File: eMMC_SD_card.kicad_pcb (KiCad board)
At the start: 4 copper layers, 100 x 74 mm, 65 parts, among them J1 SD_Card, J2 Conn_Coaxial, U1 ESP32-PICO-D4, U2 TagConnect_TC2030_ESP32

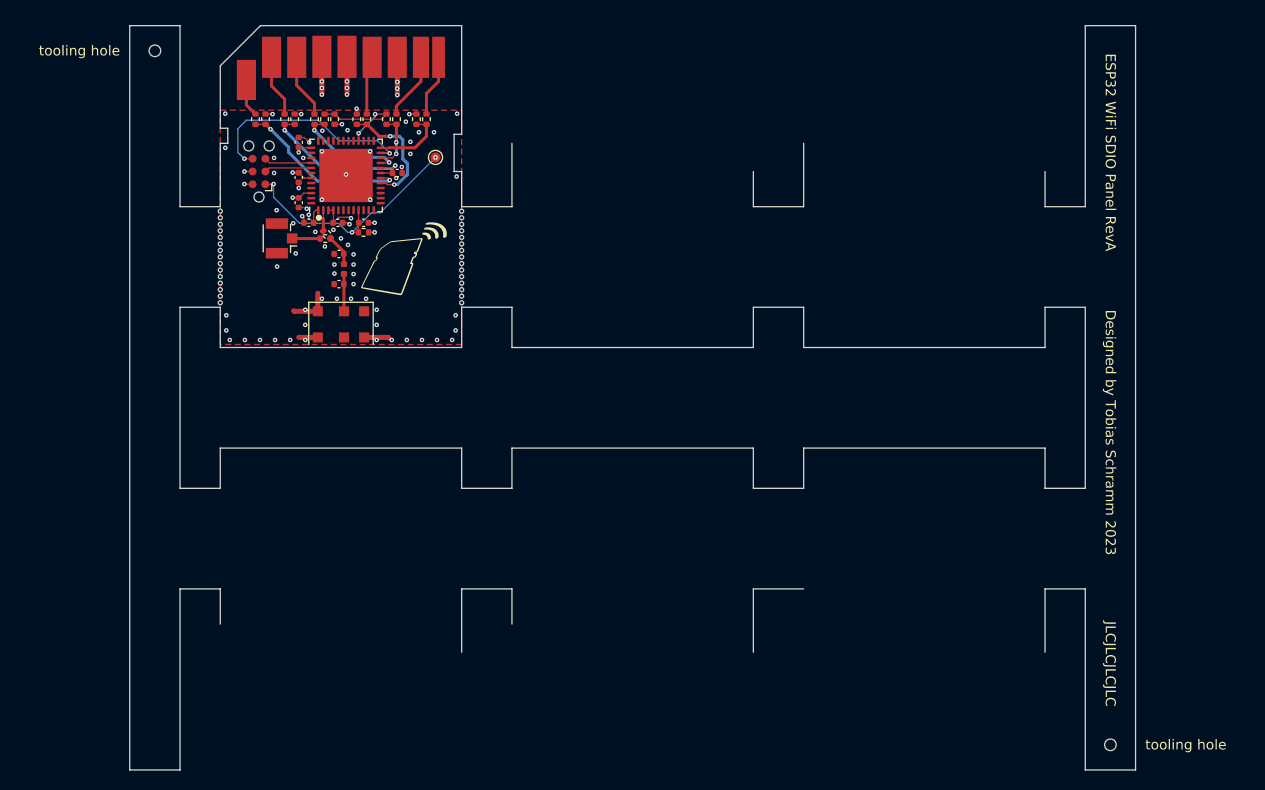
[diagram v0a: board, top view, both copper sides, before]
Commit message: Panelize
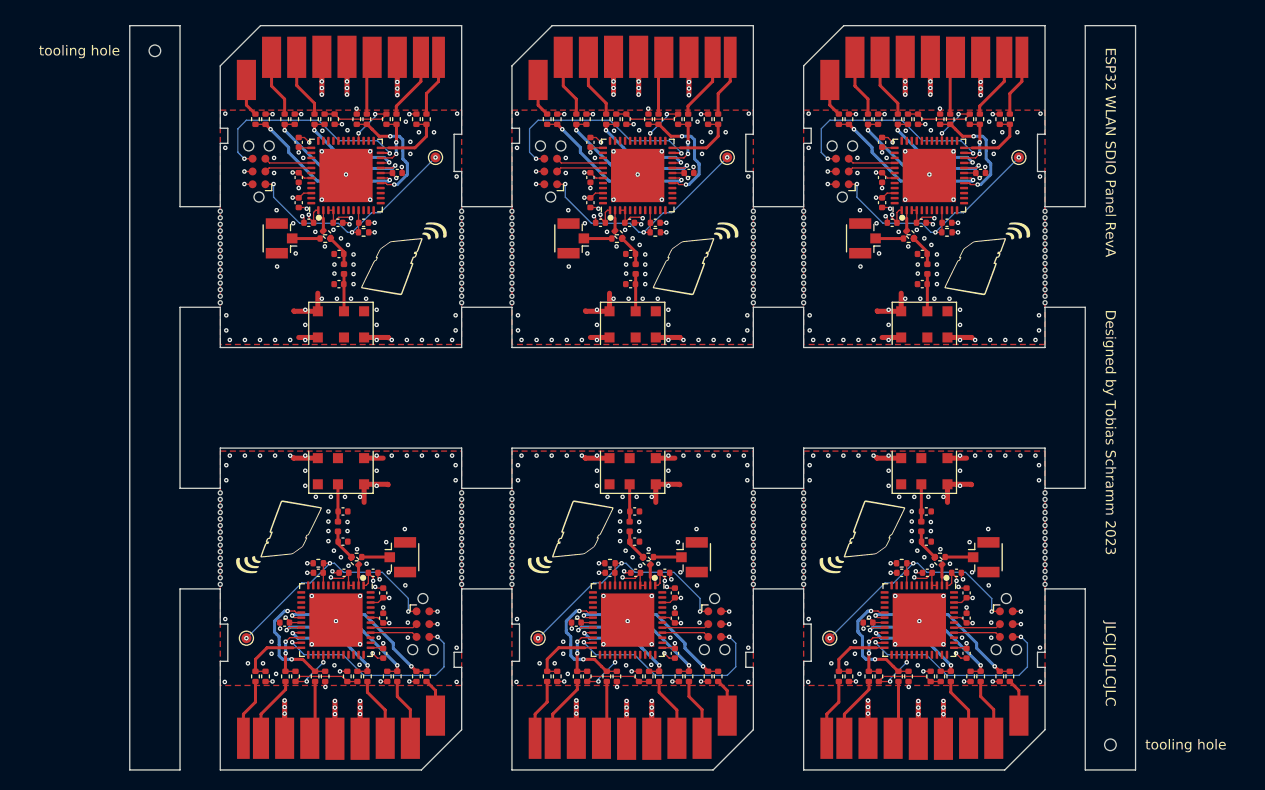
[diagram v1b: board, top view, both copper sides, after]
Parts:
- added AE2: Antenna_Chip, Antenna_antenova:SR4W035, F.Cu at (117.0, 144.3)
- added AE3: Antenna_Chip, Antenna_antenova:SR4W035, F.Cu at (175.0, 144.3)
- added AE4: Antenna_Chip, Antenna_antenova:SR4W035, F.Cu at (146.0, 129.7)
- added AE5: Antenna_Chip, Antenna_antenova:SR4W035, F.Cu at (146.0, 144.3)
- added AE6: Antenna_Chip, Antenna_antenova:SR4W035, F.Cu at (175.0, 129.7)
- added C10: 100nF, Capacitor_SMD:C_0402_1005Metric, F.Cu at (114.8, 154.4)
- added C11: 2.2uF, Capacitor_SMD:C_0402_1005Metric, F.Cu at (111.4, 159.3)
- added C12: 2.2uF, Capacitor_SMD:C_0402_1005Metric, F.Cu at (117.3, 154.4)
- added C13: 2.2uF, Capacitor_SMD:C_0402_1005Metric, F.Cu at (120.2, 154.4)
- added C14: 2.2uF, Capacitor_SMD:C_0402_1005Metric, F.Cu at (121.2, 156.4)
- added C15: 2.2uF, Capacitor_SMD:C_0402_1005Metric, F.Cu at (121.2, 158.9)
- added C16: 100nF, Capacitor_SMD:C_0402_1005Metric, F.Cu at (121.2, 162.4)
- added C17: DNP, Capacitor_SMD:C_0402_1005Metric, F.Cu at (117.2, 151.3)
- added C18: DNP, Capacitor_SMD:C_0402_1005Metric, F.Cu at (117.2, 148.3)
- added C19: 100nF, Capacitor_SMD:C_0402_1005Metric, F.Cu at (172.8, 154.4)
- added C20: 2.2uF, Capacitor_SMD:C_0402_1005Metric, F.Cu at (169.4, 159.3)
- added C21: 2.2uF, Capacitor_SMD:C_0402_1005Metric, F.Cu at (175.3, 154.4)
- added C22: 2.2uF, Capacitor_SMD:C_0402_1005Metric, F.Cu at (178.2, 154.4)
- added C23: 2.2uF, Capacitor_SMD:C_0402_1005Metric, F.Cu at (179.2, 156.4)
- added C24: 2.2uF, Capacitor_SMD:C_0402_1005Metric, F.Cu at (179.2, 158.9)
- added C25: 100nF, Capacitor_SMD:C_0402_1005Metric, F.Cu at (179.2, 162.4)
- added C26: DNP, Capacitor_SMD:C_0402_1005Metric, F.Cu at (175.2, 151.3)
- added C27: DNP, Capacitor_SMD:C_0402_1005Metric, F.Cu at (175.2, 148.3)
- added C28: 100nF, Capacitor_SMD:C_0402_1005Metric, F.Cu at (148.2, 119.6)
- added C29: 2.2uF, Capacitor_SMD:C_0402_1005Metric, F.Cu at (151.6, 114.7)
- added C30: 2.2uF, Capacitor_SMD:C_0402_1005Metric, F.Cu at (145.7, 119.6)
- added C31: 2.2uF, Capacitor_SMD:C_0402_1005Metric, F.Cu at (142.8, 119.6)
- added C32: 2.2uF, Capacitor_SMD:C_0402_1005Metric, F.Cu at (141.8, 117.6)
- added C33: 2.2uF, Capacitor_SMD:C_0402_1005Metric, F.Cu at (141.8, 115.1)
- added C34: 100nF, Capacitor_SMD:C_0402_1005Metric, F.Cu at (141.8, 111.6)
- added C35: DNP, Capacitor_SMD:C_0402_1005Metric, F.Cu at (145.8, 122.7)
- added C36: DNP, Capacitor_SMD:C_0402_1005Metric, F.Cu at (145.8, 125.7)
- added C37: 100nF, Capacitor_SMD:C_0402_1005Metric, F.Cu at (143.8, 154.4)
- added C38: 2.2uF, Capacitor_SMD:C_0402_1005Metric, F.Cu at (140.4, 159.3)
- added C39: 2.2uF, Capacitor_SMD:C_0402_1005Metric, F.Cu at (146.3, 154.4)
- added C40: 2.2uF, Capacitor_SMD:C_0402_1005Metric, F.Cu at (149.2, 154.4)
- added C41: 2.2uF, Capacitor_SMD:C_0402_1005Metric, F.Cu at (150.2, 156.4)
- added C42: 2.2uF, Capacitor_SMD:C_0402_1005Metric, F.Cu at (150.2, 158.9)
- added C43: 100nF, Capacitor_SMD:C_0402_1005Metric, F.Cu at (150.2, 162.4)
- added C44: DNP, Capacitor_SMD:C_0402_1005Metric, F.Cu at (146.2, 151.3)
- added C45: DNP, Capacitor_SMD:C_0402_1005Metric, F.Cu at (146.2, 148.3)
- added C46: 100nF, Capacitor_SMD:C_0402_1005Metric, F.Cu at (177.2, 119.6)
- added C47: 2.2uF, Capacitor_SMD:C_0402_1005Metric, F.Cu at (180.6, 114.7)
- added C48: 2.2uF, Capacitor_SMD:C_0402_1005Metric, F.Cu at (174.7, 119.6)
- added C49: 2.2uF, Capacitor_SMD:C_0402_1005Metric, F.Cu at (171.8, 119.6)
- added C50: 2.2uF, Capacitor_SMD:C_0402_1005Metric, F.Cu at (170.8, 117.6)
- added C51: 2.2uF, Capacitor_SMD:C_0402_1005Metric, F.Cu at (170.8, 115.1)
- added C52: 100nF, Capacitor_SMD:C_0402_1005Metric, F.Cu at (170.8, 111.6)
- added C53: DNP, Capacitor_SMD:C_0402_1005Metric, F.Cu at (174.8, 122.7)
- added C54: DNP, Capacitor_SMD:C_0402_1005Metric, F.Cu at (174.8, 125.7)
- added G***: LOGO, Icons:wlan_sd, F.Cu at (168.8, 150.8)
- added G***1: LOGO, Icons:wlan_sd, F.Cu at (139.8, 150.8)
- added G***1: LOGO, Icons:wlan_sd, F.Cu at (152.2, 123.2)
- added G***2: LOGO, Icons:wlan_sd, F.Cu at (110.8, 150.8)
- added G***2: LOGO, Icons:wlan_sd, F.Cu at (181.2, 123.2)
- added H100: MountingHole, Perforation:Perforation_0.4mm, F.Cu at (158.0, 121.0)
- added H101: MountingHole, Perforation:Perforation_0.4mm, F.Cu at (134.0, 121.7)
- added H102: MountingHole, Perforation:Perforation_0.4mm, F.Cu at (134.0, 122.3)
- added H103: MountingHole, Perforation:Perforation_0.4mm, F.Cu at (134.0, 123.0)
- added H104: MountingHole, Perforation:Perforation_0.4mm, F.Cu at (134.0, 123.7)
- added H105: MountingHole, Perforation:Perforation_0.4mm, F.Cu at (134.0, 124.3)
- added H106: MountingHole, Perforation:Perforation_0.4mm, F.Cu at (158.0, 121.7)
- added H107: MountingHole, Perforation:Perforation_0.4mm, F.Cu at (158.0, 122.3)
- added H108: MountingHole, Perforation:Perforation_0.4mm, F.Cu at (158.0, 123.0)
- added H109: MountingHole, Perforation:Perforation_0.4mm, F.Cu at (158.0, 123.7)
- added H110: MountingHole, Perforation:Perforation_0.4mm, F.Cu at (158.0, 124.3)
- added H111: MountingHole, Perforation:Perforation_0.4mm, F.Cu at (134.0, 125.0)
- added H112: MountingHole, Perforation:Perforation_0.4mm, F.Cu at (134.0, 125.6)
- added H113: MountingHole, Perforation:Perforation_0.4mm, F.Cu at (134.0, 126.2)
- added H114: MountingHole, Perforation:Perforation_0.4mm, F.Cu at (134.0, 126.9)
- added H115: MountingHole, Perforation:Perforation_0.4mm, F.Cu at (134.0, 127.5)
- added H116: MountingHole, Perforation:Perforation_0.4mm, F.Cu at (158.0, 125.0)
- added H117: MountingHole, Perforation:Perforation_0.4mm, F.Cu at (158.0, 125.6)
- added H118: MountingHole, Perforation:Perforation_0.4mm, F.Cu at (158.0, 126.2)
- added H119: MountingHole, Perforation:Perforation_0.4mm, F.Cu at (158.0, 126.9)
- added H120: MountingHole, Perforation:Perforation_0.4mm, F.Cu at (158.0, 127.5)
- added H121: MountingHole, Perforation:Perforation_0.4mm, F.Cu at (158.0, 155.6)
- added H122: MountingHole, Perforation:Perforation_0.4mm, F.Cu at (158.0, 154.9)
- added H123: MountingHole, Perforation:Perforation_0.4mm, F.Cu at (158.0, 154.2)
- added H124: MountingHole, Perforation:Perforation_0.4mm, F.Cu at (158.0, 153.6)
- added H125: MountingHole, Perforation:Perforation_0.4mm, F.Cu at (158.0, 152.9)
- added H126: MountingHole, Perforation:Perforation_0.4mm, F.Cu at (134.0, 155.6)
- added H127: MountingHole, Perforation:Perforation_0.4mm, F.Cu at (134.0, 154.9)
- added H128: MountingHole, Perforation:Perforation_0.4mm, F.Cu at (134.0, 154.2)
- added H129: MountingHole, Perforation:Perforation_0.4mm, F.Cu at (134.0, 153.6)
- added H130: MountingHole, Perforation:Perforation_0.4mm, F.Cu at (134.0, 152.9)
- added H131: MountingHole, Perforation:Perforation_0.4mm, F.Cu at (158.0, 152.3)
- added H132: MountingHole, Perforation:Perforation_0.4mm, F.Cu at (158.0, 151.7)
- added H133: MountingHole, Perforation:Perforation_0.4mm, F.Cu at (158.0, 151.0)
- added H134: MountingHole, Perforation:Perforation_0.4mm, F.Cu at (158.0, 150.3)
- added H135: MountingHole, Perforation:Perforation_0.4mm, F.Cu at (158.0, 149.7)
- added H136: MountingHole, Perforation:Perforation_0.4mm, F.Cu at (134.0, 152.3)
- added H137: MountingHole, Perforation:Perforation_0.4mm, F.Cu at (134.0, 151.7)
- added H138: MountingHole, Perforation:Perforation_0.4mm, F.Cu at (134.0, 151.0)
- added H139: MountingHole, Perforation:Perforation_0.4mm, F.Cu at (134.0, 150.3)
- added H140: MountingHole, Perforation:Perforation_0.4mm, F.Cu at (134.0, 149.7)
- added H141: MountingHole, Perforation:Perforation_0.4mm, F.Cu at (158.0, 149.1)
- added H142: MountingHole, Perforation:Perforation_0.4mm, F.Cu at (158.0, 148.4)
- added H143: MountingHole, Perforation:Perforation_0.4mm, F.Cu at (158.0, 147.8)
- added H144: MountingHole, Perforation:Perforation_0.4mm, F.Cu at (158.0, 147.1)
- added H145: MountingHole, Perforation:Perforation_0.4mm, F.Cu at (158.0, 146.4)
- added H146: MountingHole, Perforation:Perforation_0.4mm, F.Cu at (134.0, 149.1)
- added H147: MountingHole, Perforation:Perforation_0.4mm, F.Cu at (134.0, 148.4)
- added H148: MountingHole, Perforation:Perforation_0.4mm, F.Cu at (134.0, 147.8)
- added H149: MountingHole, Perforation:Perforation_0.4mm, F.Cu at (134.0, 147.1)
- added H150: MountingHole, Perforation:Perforation_0.4mm, F.Cu at (134.0, 146.4)
- added H151: MountingHole, Perforation:Perforation_0.4mm, F.Cu at (163.0, 118.5)
- added H152: MountingHole, Perforation:Perforation_0.4mm, F.Cu at (163.0, 119.1)
- added H153: MountingHole, Perforation:Perforation_0.4mm, F.Cu at (163.0, 119.8)
- added H154: MountingHole, Perforation:Perforation_0.4mm, F.Cu at (163.0, 120.4)
- added H155: MountingHole, Perforation:Perforation_0.4mm, F.Cu at (163.0, 121.0)
- added H156: MountingHole, Perforation:Perforation_0.4mm, F.Cu at (187.0, 118.5)
- added H157: MountingHole, Perforation:Perforation_0.4mm, F.Cu at (187.0, 119.1)
- added H158: MountingHole, Perforation:Perforation_0.4mm, F.Cu at (187.0, 119.8)
- added H159: MountingHole, Perforation:Perforation_0.4mm, F.Cu at (187.0, 120.4)
- added H160: MountingHole, Perforation:Perforation_0.4mm, F.Cu at (187.0, 121.0)
- added H161: MountingHole, Perforation:Perforation_0.4mm, F.Cu at (163.0, 121.7)
- added H162: MountingHole, Perforation:Perforation_0.4mm, F.Cu at (163.0, 122.3)
- added H163: MountingHole, Perforation:Perforation_0.4mm, F.Cu at (163.0, 123.0)
- added H164: MountingHole, Perforation:Perforation_0.4mm, F.Cu at (163.0, 123.7)
- added H165: MountingHole, Perforation:Perforation_0.4mm, F.Cu at (163.0, 124.3)
- added H166: MountingHole, Perforation:Perforation_0.4mm, F.Cu at (187.0, 121.7)
- added H167: MountingHole, Perforation:Perforation_0.4mm, F.Cu at (187.0, 122.3)
- added H168: MountingHole, Perforation:Perforation_0.4mm, F.Cu at (187.0, 123.0)
- added H169: MountingHole, Perforation:Perforation_0.4mm, F.Cu at (187.0, 123.7)
- added H170: MountingHole, Perforation:Perforation_0.4mm, F.Cu at (187.0, 124.3)
- added H171: MountingHole, Perforation:Perforation_0.4mm, F.Cu at (163.0, 125.0)
- added H172: MountingHole, Perforation:Perforation_0.4mm, F.Cu at (163.0, 125.6)
- added H173: MountingHole, Perforation:Perforation_0.4mm, F.Cu at (163.0, 126.2)
- added H174: MountingHole, Perforation:Perforation_0.4mm, F.Cu at (163.0, 126.9)
- added H175: MountingHole, Perforation:Perforation_0.4mm, F.Cu at (163.0, 127.5)
- added H176: MountingHole, Perforation:Perforation_0.4mm, F.Cu at (187.0, 125.0)
- added H177: MountingHole, Perforation:Perforation_0.4mm, F.Cu at (187.0, 125.6)
- added H178: MountingHole, Perforation:Perforation_0.4mm, F.Cu at (187.0, 126.2)
- added H179: MountingHole, Perforation:Perforation_0.4mm, F.Cu at (187.0, 126.9)
- added H180: MountingHole, Perforation:Perforation_0.4mm, F.Cu at (187.0, 127.5)
- added H31: MountingHole, Perforation:Perforation_0.4mm, F.Cu at (129.0, 155.6)
- added H32: MountingHole, Perforation:Perforation_0.4mm, F.Cu at (129.0, 154.9)
- added H33: MountingHole, Perforation:Perforation_0.4mm, F.Cu at (129.0, 154.2)
- added H34: MountingHole, Perforation:Perforation_0.4mm, F.Cu at (129.0, 153.6)
- added H35: MountingHole, Perforation:Perforation_0.4mm, F.Cu at (129.0, 152.9)
- added H36: MountingHole, Perforation:Perforation_0.4mm, F.Cu at (105.0, 155.6)
- added H37: MountingHole, Perforation:Perforation_0.4mm, F.Cu at (105.0, 154.9)
- added H38: MountingHole, Perforation:Perforation_0.4mm, F.Cu at (105.0, 154.2)
- added H39: MountingHole, Perforation:Perforation_0.4mm, F.Cu at (105.0, 153.6)
- added H40: MountingHole, Perforation:Perforation_0.4mm, F.Cu at (105.0, 152.9)
- added H41: MountingHole, Perforation:Perforation_0.4mm, F.Cu at (129.0, 152.3)
- added H42: MountingHole, Perforation:Perforation_0.4mm, F.Cu at (129.0, 151.7)
- added H43: MountingHole, Perforation:Perforation_0.4mm, F.Cu at (129.0, 151.0)
- added H44: MountingHole, Perforation:Perforation_0.4mm, F.Cu at (129.0, 150.3)
- added H45: MountingHole, Perforation:Perforation_0.4mm, F.Cu at (129.0, 149.7)
- added H46: MountingHole, Perforation:Perforation_0.4mm, F.Cu at (105.0, 152.3)
- added H47: MountingHole, Perforation:Perforation_0.4mm, F.Cu at (105.0, 151.7)
- added H48: MountingHole, Perforation:Perforation_0.4mm, F.Cu at (105.0, 151.0)
- added H49: MountingHole, Perforation:Perforation_0.4mm, F.Cu at (105.0, 150.3)
- added H50: MountingHole, Perforation:Perforation_0.4mm, F.Cu at (105.0, 149.7)
- added H51: MountingHole, Perforation:Perforation_0.4mm, F.Cu at (129.0, 149.1)
- added H52: MountingHole, Perforation:Perforation_0.4mm, F.Cu at (129.0, 148.4)
- added H53: MountingHole, Perforation:Perforation_0.4mm, F.Cu at (129.0, 147.8)
- added H54: MountingHole, Perforation:Perforation_0.4mm, F.Cu at (129.0, 147.1)
- added H55: MountingHole, Perforation:Perforation_0.4mm, F.Cu at (129.0, 146.4)
- added H56: MountingHole, Perforation:Perforation_0.4mm, F.Cu at (105.0, 149.1)
- added H57: MountingHole, Perforation:Perforation_0.4mm, F.Cu at (105.0, 148.4)
- added H58: MountingHole, Perforation:Perforation_0.4mm, F.Cu at (105.0, 147.8)
- added H59: MountingHole, Perforation:Perforation_0.4mm, F.Cu at (105.0, 147.1)
- added H60: MountingHole, Perforation:Perforation_0.4mm, F.Cu at (105.0, 146.4)
- added H61: MountingHole, Perforation:Perforation_0.4mm, F.Cu at (187.0, 155.6)
- added H62: MountingHole, Perforation:Perforation_0.4mm, F.Cu at (187.0, 154.9)
- added H63: MountingHole, Perforation:Perforation_0.4mm, F.Cu at (187.0, 154.2)
- added H64: MountingHole, Perforation:Perforation_0.4mm, F.Cu at (187.0, 153.6)
- added H65: MountingHole, Perforation:Perforation_0.4mm, F.Cu at (187.0, 152.9)
- added H66: MountingHole, Perforation:Perforation_0.4mm, F.Cu at (163.0, 155.6)
- added H67: MountingHole, Perforation:Perforation_0.4mm, F.Cu at (163.0, 154.9)
- added H68: MountingHole, Perforation:Perforation_0.4mm, F.Cu at (163.0, 154.2)
- added H69: MountingHole, Perforation:Perforation_0.4mm, F.Cu at (163.0, 153.6)
- added H70: MountingHole, Perforation:Perforation_0.4mm, F.Cu at (163.0, 152.9)
- added H71: MountingHole, Perforation:Perforation_0.4mm, F.Cu at (187.0, 152.3)
- added H72: MountingHole, Perforation:Perforation_0.4mm, F.Cu at (187.0, 151.7)
- added H73: MountingHole, Perforation:Perforation_0.4mm, F.Cu at (187.0, 151.0)
- added H74: MountingHole, Perforation:Perforation_0.4mm, F.Cu at (187.0, 150.3)
- added H75: MountingHole, Perforation:Perforation_0.4mm, F.Cu at (187.0, 149.7)
- added H76: MountingHole, Perforation:Perforation_0.4mm, F.Cu at (163.0, 152.3)
- added H77: MountingHole, Perforation:Perforation_0.4mm, F.Cu at (163.0, 151.7)
- added H78: MountingHole, Perforation:Perforation_0.4mm, F.Cu at (163.0, 151.0)
- added H79: MountingHole, Perforation:Perforation_0.4mm, F.Cu at (163.0, 150.3)
- added H80: MountingHole, Perforation:Perforation_0.4mm, F.Cu at (163.0, 149.7)
- added H81: MountingHole, Perforation:Perforation_0.4mm, F.Cu at (187.0, 149.1)
- added H82: MountingHole, Perforation:Perforation_0.4mm, F.Cu at (187.0, 148.4)
- added H83: MountingHole, Perforation:Perforation_0.4mm, F.Cu at (187.0, 147.8)
- added H84: MountingHole, Perforation:Perforation_0.4mm, F.Cu at (187.0, 147.1)
- added H85: MountingHole, Perforation:Perforation_0.4mm, F.Cu at (187.0, 146.4)
- added H86: MountingHole, Perforation:Perforation_0.4mm, F.Cu at (163.0, 149.1)
- added H87: MountingHole, Perforation:Perforation_0.4mm, F.Cu at (163.0, 148.4)
- added H88: MountingHole, Perforation:Perforation_0.4mm, F.Cu at (163.0, 147.8)
- added H89: MountingHole, Perforation:Perforation_0.4mm, F.Cu at (163.0, 147.1)
- added H90: MountingHole, Perforation:Perforation_0.4mm, F.Cu at (163.0, 146.4)
- added H91: MountingHole, Perforation:Perforation_0.4mm, F.Cu at (134.0, 118.5)
- added H92: MountingHole, Perforation:Perforation_0.4mm, F.Cu at (134.0, 119.1)
- added H93: MountingHole, Perforation:Perforation_0.4mm, F.Cu at (134.0, 119.8)
- added H94: MountingHole, Perforation:Perforation_0.4mm, F.Cu at (134.0, 120.4)
- added H95: MountingHole, Perforation:Perforation_0.4mm, F.Cu at (134.0, 121.0)
- added H96: MountingHole, Perforation:Perforation_0.4mm, F.Cu at (158.0, 118.5)
- added H97: MountingHole, Perforation:Perforation_0.4mm, F.Cu at (158.0, 119.1)
- added H98: MountingHole, Perforation:Perforation_0.4mm, F.Cu at (158.0, 119.8)
- added H99: MountingHole, Perforation:Perforation_0.4mm, F.Cu at (158.0, 120.4)
- added J10: Conn_Coaxial, Connector_Coaxial:U.FL_Hirose_U.FL-R-SMT-1_Vertical, F.Cu at (151.9, 152.8)
- added J11: SD_Card, Connector_PCB_Edge_SD:SD, F.Cu at (163.0, 100.0)
- added J12: Conn_Coaxial, Connector_Coaxial:U.FL_Hirose_U.FL-R-SMT-1_Vertical, F.Cu at (169.1, 121.2)
- added J3: SD_Card, Connector_PCB_Edge_SD:SD, F.Cu at (129.0, 174.0)
- added J4: Conn_Coaxial, Connector_Coaxial:U.FL_Hirose_U.FL-R-SMT-1_Vertical, F.Cu at (122.9, 152.8)
- added J5: SD_Card, Connector_PCB_Edge_SD:SD, F.Cu at (187.0, 174.0)
- added J6: Conn_Coaxial, Connector_Coaxial:U.FL_Hirose_U.FL-R-SMT-1_Vertical, F.Cu at (180.9, 152.8)
- added J7: SD_Card, Connector_PCB_Edge_SD:SD, F.Cu at (134.0, 100.0)
- added J8: Conn_Coaxial, Connector_Coaxial:U.FL_Hirose_U.FL-R-SMT-1_Vertical, F.Cu at (140.1, 121.2)
- added J9: SD_Card, Connector_PCB_Edge_SD:SD, F.Cu at (158.0, 174.0)
- added L2: 0R, Inductor_SMD:L_0402_1005Metric, F.Cu at (116.7, 149.8)
- added L3: 0R, Inductor_SMD:L_0402_1005Metric, F.Cu at (174.7, 149.8)
- added L4: 0R, Inductor_SMD:L_0402_1005Metric, F.Cu at (146.3, 124.2)
- added L5: 0R, Inductor_SMD:L_0402_1005Metric, F.Cu at (145.7, 149.8)
- added L6: 0R, Inductor_SMD:L_0402_1005Metric, F.Cu at (175.3, 124.2)
- added R17: 33R, Resistor_SMD:R_0402_1005Metric, F.Cu at (125.5, 164.7)
- added R18: 33R, Resistor_SMD:R_0402_1005Metric, F.Cu at (114.4, 164.7)
- added R19: 33R, Resistor_SMD:R_0402_1005Metric, F.Cu at (122.6, 164.7)
- added R20: 33R, Resistor_SMD:R_0402_1005Metric, F.Cu at (111.5, 164.7)
- added R21: 33R, Resistor_SMD:R_0402_1005Metric, F.Cu at (119.6, 164.7)
- added R22: 33R, Resistor_SMD:R_0402_1005Metric, F.Cu at (108.5, 164.7)
- added R23: 10k, Resistor_SMD:R_0402_1005Metric, F.Cu at (124.5, 164.7)
- added R24: 10k, Resistor_SMD:R_0402_1005Metric, F.Cu at (121.6, 164.7)
- added R25: 10k, Resistor_SMD:R_0402_1005Metric, F.Cu at (115.4, 164.7)
- added R26: 10k, Resistor_SMD:R_0402_1005Metric, F.Cu at (109.5, 164.7)
- added R27: 10k, Resistor_SMD:R_0402_1005Metric, F.Cu at (114.8, 153.4)
- added R28: 0R, Resistor_SMD:R_0402_1005Metric, F.Cu at (118.4, 153.2)
- added R29: 0R, Resistor_SMD:R_0402_1005Metric, F.Cu at (118.6, 152.8)
- added R30: 10k, Resistor_SMD:R_0402_1005Metric, F.Cu at (112.5, 164.7)
- added R31: 10k, Resistor_SMD:R_0402_1005Metric, F.Cu at (118.6, 164.7)
- added R32: 10k, Resistor_SMD:R_0402_1005Metric, F.Cu at (117.6, 164.7)
- added R33: 33R, Resistor_SMD:R_0402_1005Metric, F.Cu at (183.5, 164.7)
- added R34: 33R, Resistor_SMD:R_0402_1005Metric, F.Cu at (172.4, 164.7)
- added R35: 33R, Resistor_SMD:R_0402_1005Metric, F.Cu at (180.6, 164.7)
- added R36: 33R, Resistor_SMD:R_0402_1005Metric, F.Cu at (169.5, 164.7)
- added R37: 33R, Resistor_SMD:R_0402_1005Metric, F.Cu at (177.6, 164.7)
- added R38: 33R, Resistor_SMD:R_0402_1005Metric, F.Cu at (166.5, 164.7)
- added R39: 10k, Resistor_SMD:R_0402_1005Metric, F.Cu at (182.5, 164.7)
- added R40: 10k, Resistor_SMD:R_0402_1005Metric, F.Cu at (179.6, 164.7)
- added R41: 10k, Resistor_SMD:R_0402_1005Metric, F.Cu at (173.4, 164.7)
- added R42: 10k, Resistor_SMD:R_0402_1005Metric, F.Cu at (167.5, 164.7)
- added R43: 10k, Resistor_SMD:R_0402_1005Metric, F.Cu at (172.8, 153.4)
- added R44: 0R, Resistor_SMD:R_0402_1005Metric, F.Cu at (176.4, 153.2)
- added R45: 0R, Resistor_SMD:R_0402_1005Metric, F.Cu at (176.6, 152.8)
- added R46: 10k, Resistor_SMD:R_0402_1005Metric, F.Cu at (170.5, 164.7)
- added R47: 10k, Resistor_SMD:R_0402_1005Metric, F.Cu at (176.6, 164.7)
- added R48: 10k, Resistor_SMD:R_0402_1005Metric, F.Cu at (175.6, 164.7)
- added R49: 33R, Resistor_SMD:R_0402_1005Metric, F.Cu at (137.5, 109.3)
- added R50: 33R, Resistor_SMD:R_0402_1005Metric, F.Cu at (148.6, 109.3)
- added R51: 33R, Resistor_SMD:R_0402_1005Metric, F.Cu at (140.4, 109.3)
- added R52: 33R, Resistor_SMD:R_0402_1005Metric, F.Cu at (151.5, 109.3)
- added R53: 33R, Resistor_SMD:R_0402_1005Metric, F.Cu at (143.4, 109.3)
- added R54: 33R, Resistor_SMD:R_0402_1005Metric, F.Cu at (154.5, 109.3)
- added R55: 10k, Resistor_SMD:R_0402_1005Metric, F.Cu at (138.5, 109.3)
- added R56: 10k, Resistor_SMD:R_0402_1005Metric, F.Cu at (141.4, 109.3)
- added R57: 10k, Resistor_SMD:R_0402_1005Metric, F.Cu at (147.6, 109.3)
- added R58: 10k, Resistor_SMD:R_0402_1005Metric, F.Cu at (153.5, 109.3)
- added R59: 10k, Resistor_SMD:R_0402_1005Metric, F.Cu at (148.2, 120.5)
- added R60: 0R, Resistor_SMD:R_0402_1005Metric, F.Cu at (144.6, 120.8)
- added R61: 0R, Resistor_SMD:R_0402_1005Metric, F.Cu at (144.4, 121.2)
- added R62: 10k, Resistor_SMD:R_0402_1005Metric, F.Cu at (150.5, 109.3)
- added R63: 10k, Resistor_SMD:R_0402_1005Metric, F.Cu at (144.4, 109.3)
- added R64: 10k, Resistor_SMD:R_0402_1005Metric, F.Cu at (145.4, 109.3)
- added R65: 33R, Resistor_SMD:R_0402_1005Metric, F.Cu at (154.5, 164.7)
- added R66: 33R, Resistor_SMD:R_0402_1005Metric, F.Cu at (143.4, 164.7)
- added R67: 33R, Resistor_SMD:R_0402_1005Metric, F.Cu at (151.6, 164.7)
- added R68: 33R, Resistor_SMD:R_0402_1005Metric, F.Cu at (140.5, 164.7)
- added R69: 33R, Resistor_SMD:R_0402_1005Metric, F.Cu at (148.6, 164.7)
- added R70: 33R, Resistor_SMD:R_0402_1005Metric, F.Cu at (137.5, 164.7)
- added R71: 10k, Resistor_SMD:R_0402_1005Metric, F.Cu at (153.5, 164.7)
- added R72: 10k, Resistor_SMD:R_0402_1005Metric, F.Cu at (150.6, 164.7)
- added R73: 10k, Resistor_SMD:R_0402_1005Metric, F.Cu at (144.4, 164.7)
- added R74: 10k, Resistor_SMD:R_0402_1005Metric, F.Cu at (138.5, 164.7)
- added R75: 10k, Resistor_SMD:R_0402_1005Metric, F.Cu at (143.8, 153.4)
- added R76: 0R, Resistor_SMD:R_0402_1005Metric, F.Cu at (147.4, 153.2)
- added R77: 0R, Resistor_SMD:R_0402_1005Metric, F.Cu at (147.6, 152.8)
- added R78: 10k, Resistor_SMD:R_0402_1005Metric, F.Cu at (141.5, 164.7)
- added R79: 10k, Resistor_SMD:R_0402_1005Metric, F.Cu at (147.6, 164.7)
- added R80: 10k, Resistor_SMD:R_0402_1005Metric, F.Cu at (146.6, 164.7)
- added R81: 33R, Resistor_SMD:R_0402_1005Metric, F.Cu at (166.5, 109.3)
- added R82: 33R, Resistor_SMD:R_0402_1005Metric, F.Cu at (177.6, 109.3)
- added R83: 33R, Resistor_SMD:R_0402_1005Metric, F.Cu at (169.4, 109.3)
- added R84: 33R, Resistor_SMD:R_0402_1005Metric, F.Cu at (180.5, 109.3)
- added R85: 33R, Resistor_SMD:R_0402_1005Metric, F.Cu at (172.4, 109.3)
- added R86: 33R, Resistor_SMD:R_0402_1005Metric, F.Cu at (183.5, 109.3)
- added R87: 10k, Resistor_SMD:R_0402_1005Metric, F.Cu at (167.5, 109.3)
- added R88: 10k, Resistor_SMD:R_0402_1005Metric, F.Cu at (170.4, 109.3)
- added R89: 10k, Resistor_SMD:R_0402_1005Metric, F.Cu at (176.6, 109.3)
- added R90: 10k, Resistor_SMD:R_0402_1005Metric, F.Cu at (182.5, 109.3)
- added R91: 10k, Resistor_SMD:R_0402_1005Metric, F.Cu at (177.2, 120.5)
- added R92: 0R, Resistor_SMD:R_0402_1005Metric, F.Cu at (173.6, 120.8)
- added R93: 0R, Resistor_SMD:R_0402_1005Metric, F.Cu at (173.4, 121.2)
- added R94: 10k, Resistor_SMD:R_0402_1005Metric, F.Cu at (179.5, 109.3)
- added R95: 10k, Resistor_SMD:R_0402_1005Metric, F.Cu at (173.4, 109.3)
- added R96: 10k, Resistor_SMD:R_0402_1005Metric, F.Cu at (174.4, 109.3)
- added TP2: RESET, TestPoint:TestPoint_Pad_D1.0mm, F.Cu at (107.6, 160.9)
- added TP3: RESET, TestPoint:TestPoint_Pad_D1.0mm, F.Cu at (165.6, 160.9)
- added TP4: RESET, TestPoint:TestPoint_Pad_D1.0mm, F.Cu at (155.4, 113.1)
- added TP5: RESET, TestPoint:TestPoint_Pad_D1.0mm, F.Cu at (136.6, 160.9)
- added TP6: RESET, TestPoint:TestPoint_Pad_D1.0mm, F.Cu at (184.4, 113.1)
- added U10: ESP32-PICO-D4, Package_DFN_QFN:QFN-48-1EP_7x7mm_P0.5mm_EP5.3x5.3mm, F.Cu at (145.5, 159.1)
- added U11: TagConnect_TC2030_ESP32, Connector:Tag-Connect_TC2030-IDC-NL_2x03_P1.27mm_Vertical, F.Cu at (166.8, 114.5)
- added U12: ESP32-PICO-D4, Package_DFN_QFN:QFN-48-1EP_7x7mm_P0.5mm_EP5.3x5.3mm, F.Cu at (175.5, 114.9)
- added U3: TagConnect_TC2030_ESP32, Connector:Tag-Connect_TC2030-IDC-NL_2x03_P1.27mm_Vertical, F.Cu at (125.2, 159.5)
- added U4: ESP32-PICO-D4, Package_DFN_QFN:QFN-48-1EP_7x7mm_P0.5mm_EP5.3x5.3mm, F.Cu at (116.5, 159.1)
- added U5: TagConnect_TC2030_ESP32, Connector:Tag-Connect_TC2030-IDC-NL_2x03_P1.27mm_Vertical, F.Cu at (183.2, 159.5)
- added U6: ESP32-PICO-D4, Package_DFN_QFN:QFN-48-1EP_7x7mm_P0.5mm_EP5.3x5.3mm, F.Cu at (174.5, 159.1)
- added U7: TagConnect_TC2030_ESP32, Connector:Tag-Connect_TC2030-IDC-NL_2x03_P1.27mm_Vertical, F.Cu at (137.8, 114.5)
- added U8: ESP32-PICO-D4, Package_DFN_QFN:QFN-48-1EP_7x7mm_P0.5mm_EP5.3x5.3mm, F.Cu at (146.5, 114.9)
- added U9: TagConnect_TC2030_ESP32, Connector:Tag-Connect_TC2030-IDC-NL_2x03_P1.27mm_Vertical, F.Cu at (154.2, 159.5)
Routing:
- net GND: track 23.0 -> 138.0 mm, vias 73 -> 438
- net +3V3: track 22.0 -> 132.3 mm, vias 15 -> 90
- net /Adapter 5/EN: track 0.00 -> 25.7 mm, vias 0 -> 3
- net /Adapter 3/EN: track 0.00 -> 25.7 mm, vias 0 -> 3
- net /Adapter 2/EN: track 0.00 -> 25.7 mm, vias 0 -> 3
- net /Adapter 6/EN: track 0.00 -> 25.7 mm, vias 0 -> 3
- net /Adapter 4/EN: track 0.00 -> 25.7 mm, vias 0 -> 3
- net /Adapter 6/IO0: track 0.00 -> 22.3 mm, vias 0 -> 2
- net /Adapter 4/IO0: track 0.00 -> 22.3 mm, vias 0 -> 2
- net /Adapter 5/IO0: track 0.00 -> 22.3 mm, vias 0 -> 2
- net /Adapter 3/IO0: track 0.00 -> 22.3 mm, vias 0 -> 2
- net /Adapter 2/IO0: track 0.00 -> 22.3 mm, vias 0 -> 2
- net /Adapter 6/DAT2: track 0.00 -> 17.1 mm, vias 0 -> 2
- net /Adapter 4/DAT2: track 0.00 -> 17.1 mm, vias 0 -> 2
- net /Adapter 5/DAT2: track 0.00 -> 17.1 mm, vias 0 -> 2
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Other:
- outline, holes or cut-outs redrawn
- board text added: "ESP32 WLAN SDIO Card RevA"
- board text added: "ESP32 WLAN SDIO Panel RevA"
- board text removed: "ESP32 WLAN SDIO card RevA"
- board text removed: "ESP32 WiFi SDIO Panel RevA"
